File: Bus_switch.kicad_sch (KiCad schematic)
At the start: 8 parts, among them J3 Conn_01x04_Pin, U1 SN74CB3Q3384APW

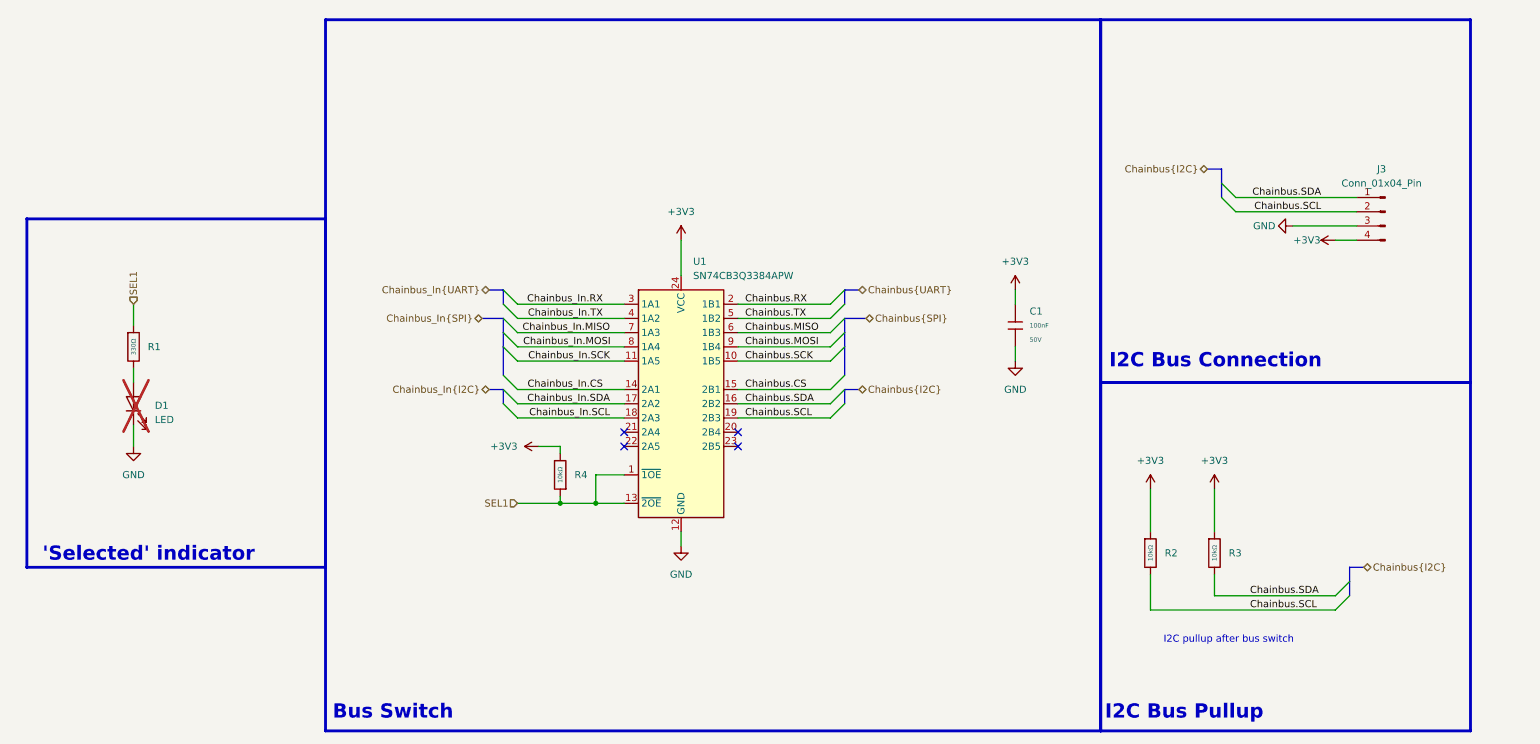
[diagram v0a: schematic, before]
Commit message: updated bus switch to sensible one
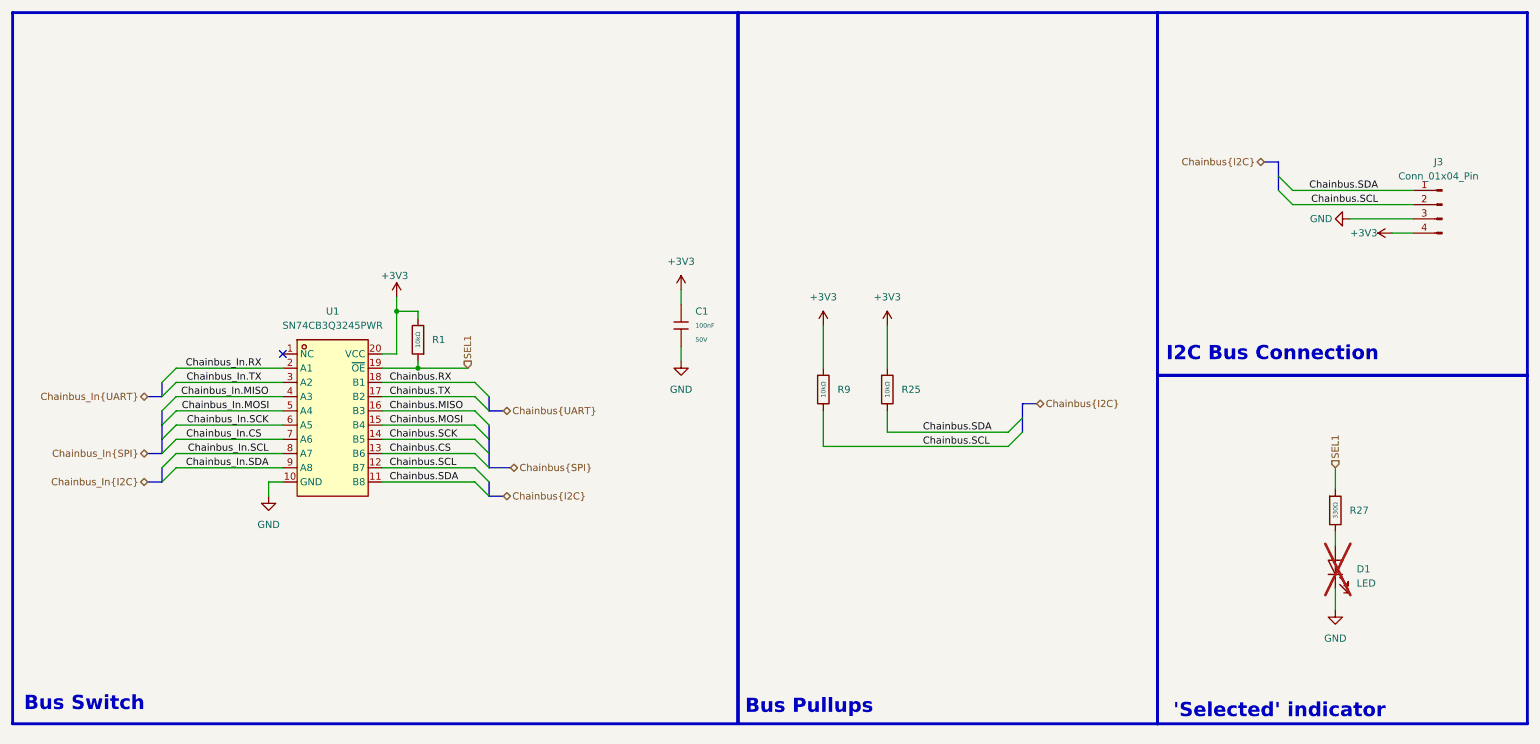
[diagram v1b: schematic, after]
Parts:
- removed U1: SN74CB3Q3384APW, Package_SO:TSSOP-24_4.4x7.8mm_P0.65mm, symbol 74xx:SN74CB3Q3384APW
- added U1: SN74CB3Q3245PWR, SN74CB3Q3245PWR:TSSOP-20_L6.5-W4.4-P0.65-LS6.4-BL, symbol SN74CB3Q3245PWR:SN74CB3Q3245PWR
- renumbered R4 to R1, R3 to R25, R1 to R27, R2 to R9
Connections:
- net +3V3: now also U1.20 (VCC)
- net Chainbus.CS: now also U1.13 (B6)
- net Chainbus.MISO: now also U1.16 (B3)
- net Chainbus.MOSI: now also U1.15 (B4)
- net Chainbus.RX: now also U1.18 (B1)
- net Chainbus.SCK: now also U1.14 (B5)
- net Chainbus.SCL: now also U1.12 (B7)
- net Chainbus.SDA: now also U1.11 (B8)
- net Chainbus.TX: now also U1.17 (B2)
- net Chainbus_In.CS: now also U1.7 (A6)
- net Chainbus_In.MISO: now also U1.4 (A3)
- net Chainbus_In.MOSI: now also U1.5 (A4)
- net Chainbus_In.RX: now also U1.2 (A1)
- net Chainbus_In.SCK: now also U1.6 (A5)
- net Chainbus_In.SCL: now also U1.8 (A7)
- net Chainbus_In.SDA: now also U1.9 (A8)
- net Chainbus_In.TX: now also U1.3 (A2)
- net GND: now also U1.10 (GND)
- net SEL1: now also U1.19 (~{OE})
- no-connect marks 4 -> 1
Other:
- note added: "Bus Pullups"
- note removed: "I2C Bus Pullup"
- note removed: "I2C pullup after bus switch"
- title: MMS3 Stepper Controler -> MMS3 Hat template small (Change Me)
- moved on the sheet: C1, D1, J3, R1, R25, R27, R9
